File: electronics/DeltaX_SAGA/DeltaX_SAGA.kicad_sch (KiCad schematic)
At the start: 73 parts, among them J1 USB_B_Micro, J10 Motor3_Encoder, J11 M12, J12 M21, J13 M22, J14 M31, J15 M33, J16 Thrower+, J17 Thrower-, J2 Programmer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

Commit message: schematic updated
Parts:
- L1: value 7.6uH -> 6.8uH
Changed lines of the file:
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@@
       (effects (font (size 1.27 1.27)) (justify left))
     )
-    (property "Value" "7.6uH" (id 1) (at 232.6132 68.8594 90)
+    (property "Value" "6.8uH" (id 1) (at 232.6132 68.8594 90)
       (effects (font (size 1.27 1.27)) (justify left))
     )
@@
     )
     (path "/69cf5053-6b07-4bfe-8c3a-5438a0737fc8"
-      (reference "L1") (unit 1) (value "7.6uH") (footprint "SRP6060FA5R6M:SRP6060FA5R6M")
+      (reference "L1") (unit 1) (value "6.8uH") (footprint "SRP6060FA5R6M:SRP6060FA5R6M")
     )
     (path "/a41829a6-8151-41c8-b9a0-f89cf565cdea"

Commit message: Schematic updated
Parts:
- L1: value 6.8uH -> 5.6uH
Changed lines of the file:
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@@
       (effects (font (size 1.27 1.27)) (justify left))
     )
-    (property "Value" "6.8uH" (id 1) (at 232.6132 68.8594 90)
+    (property "Value" "5.6uH" (id 1) (at 232.6132 68.8594 90)
       (effects (font (size 1.27 1.27)) (justify left))
     )
@@
     )
     (path "/69cf5053-6b07-4bfe-8c3a-5438a0737fc8"
-      (reference "L1") (unit 1) (value "6.8uH") (footprint "SRP6060FA5R6M:SRP6060FA5R6M")
+      (reference "L1") (unit 1) (value "5.6uH") (footprint "SRP6060FA5R6M:SRP6060FA5R6M")
     )
     (path "/a41829a6-8151-41c8-b9a0-f89cf565cdea"

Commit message: Schematic updated
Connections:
- net +5VD: now also J3.2 (Pin_2); no longer J3.1 (Pin_1)
- net Servo_PWM_Isolated: now also J3.1 (Pin_1); no longer J3.2 (Pin_2)
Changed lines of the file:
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@@
     (stroke (width 0) (type default) (color 0 0 0 0))
   )
-  (wire (pts (xy 343.408 228.6) (xy 343.408 226.822))
+  (wire (pts (xy 338.836 228.6) (xy 338.836 225.2726))
     (stroke (width 0) (type default) (color 0 0 0 0))
   )
@@
     (stroke (width 0) (type default) (color 0 0 0 0))
   )
-  (wire (pts (xy 337.312 228.6) (xy 343.408 228.6))
+  (wire (pts (xy 337.312 231.14) (xy 343.408 231.14))
     (stroke (width 0) (type default) (color 0 0 0 0))
   )
@@
     (stroke (width 0) (type default) (color 0 0 0 0))
   )
+  (wire (pts (xy 338.836 225.2726) (xy 339.979 225.2726))
+    (stroke (width 0) (type default) (color 0 0 0 0))
+  )
   (wire (pts (xy 345.821 82.3976) (xy 345.821 84.963))
     (stroke (width 0) (type default) (color 0 0 0 0))
@@
   )
   (polyline (pts (xy 390.017 174.625) (xy 390.017 147.574))
+    (stroke (width 0) (type default) (color 0 0 0 0))
+  )
+  (wire (pts (xy 337.312 228.6) (xy 338.836 228.6))
     (stroke (width 0) (type default) (color 0 0 0 0))
   )
@@
     (effects (font (size 1.27 1.27)) (justify left bottom))
   )
-  (label "Servo_PWM_Isolated" (at 337.312 231.14 0)
-    (effects (font (size 1.27 1.27)) (justify left bottom))
+  (label "Servo_PWM_Isolated" (at 339.979 225.2726 0)
+    (effects (font (size 1 1)) (justify left bottom))
   )
   (label "Motor3_OUT1" (at 289.3568 41.7322 180)
@@
     (pin "2")
   )
-  (symbol (lib_id "power:+5VD") (at 343.408 226.822 0) (unit 1)
-    (in_bom yes) (on_board yes)
-    (property "Reference" "#PWR014" (id 0) (at 343.408 230.632 0)
-      (effects (font (size 1.27 1.27)) hide)
-    )
-    (property "Value" "+5VD" (id 1) (at 343.154 223.012 0))
-    (property "Footprint" "" (id 2) (at 343.408 226.822 0)
-      (effects (font (size 1.27 1.27)) hide)
-    )
-    (property "Datasheet" "" (id 3) (at 343.408 226.822 0)
-      (effects (font (size 1.27 1.27)) hide)
-    )
+  (symbol (lib_id "power:+5VD") (at 343.408 231.14 0) (unit 1)
+    (in_bom yes) (on_board yes)
+    (property "Reference" "#PWR014" (id 0) (at 343.408 234.95 0)
+      (effects (font (size 1.27 1.27)) hide)
+    )
+    (property "Value" "+5VD" (id 1) (at 343.154 227.33 0))
+    (property "Footprint" "" (id 2) (at 343.408 231.14 0)
+      (effects (font (size 1.27 1.27)) hide)
+    )
+    (property "Datasheet" "" (id 3) (at 343.408 231.14 0)
+      (effects (font (size 1.27 1.27)) hide)
+    )

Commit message: Labels and orientations of certain components updated in schematic
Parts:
- J10: value Motor3_Encoder -> M3_Encoder
- J16: value Thrower+ -> THRWR+
- J17: value Thrower- -> THRWR-
- J5: value Battery+ -> BAT+
- J6: value Thrower Signal -> Thrower
- J7: value Battery- -> BAT-
- J8: value Motor1_Encoder -> M1_Encoder
- J9: value Motor2_Encoder -> M2_Encoder
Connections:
- net Servo_PWM: now also U3.25 (PA15), U7.3 (INA1); no longer U3.7 (PA2), U8.2 (IN1)
- net Servo_PWM_Isolated: now also U7.14 (INB1); no longer U8.7 (OUT1)
- net Thrower_PWM: now also U3.7 (PA2), U8.2 (IN1); no longer U3.25 (PA15), U7.3 (INA1)
- net Thrower_PWM_Isolated: now also U8.7 (OUT1); no longer U7.14 (INB1)
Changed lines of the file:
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@@
     (effects (font (size 1.27 1.27)) (justify right bottom))
   )
-  (label "Thrower_PWM" (at 346.6846 42.3926 180)
+  (label "Thrower_PWM" (at 346.7354 126.746 180)
     (effects (font (size 1.27 1.27)) (justify right bottom))
   )
@@
     (effects (font (size 1.27 1.27)) (justify right bottom))
   )
-  (label "Thrower_PWM" (at 76.0984 219.6084 0)
-    (effects (font (size 1.27 1.27)) (justify left bottom))
+  (label "Thrower_PWM" (at 45.6184 214.5284 180)
+    (effects (font (size 1.27 1.27)) (justify right bottom))
   )
   (label "Motor3_DIR" (at 345.821 98.425 180)
@@
     (effects (font (size 1.27 1.27)) (justify left bottom))
   )
-  (label "Thrower_PWM_Isolated" (at 368.2746 42.3926 0)
+  (label "Thrower_PWM_Isolated" (at 367.0554 126.746 0)
     (effects (font (size 1.27 1.27)) (justify left bottom))
   )
@@
     (effects (font (size 1.27 1.27)) (justify right bottom))
   )
-  (label "Servo_PWM" (at 45.6184 214.5284 180)
-    (effects (font (size 1.27 1.27)) (justify right bottom))
+  (label "Servo_PWM" (at 76.0984 219.6084 0)
+    (effects (font (size 1.27 1.27)) (justify left bottom))
   )
   (label "Motor1_DIR" (at 76.0984 237.1344 0)
@@
     (effects (font (size 1.27 1.27)) (justify right bottom))
   )
-  (label "Servo_PWM_Isolated" (at 367.0554 126.746 0)
+  (label "Servo_PWM_Isolated" (at 368.2746 42.3926 0)
     (effects (font (size 1.27 1.27)) (justify left bottom))
   )
@@
     (effects (font (size 1.27 1.27)) (justify right bottom))
   )
-  (label "Servo_PWM" (at 346.7354 126.746 180)
+  (label "Servo_PWM" (at 346.6846 42.3926 180)
     (effects (font (size 1.27 1.27)) (justify right bottom))
   )
@@
       (effects (font (size 1.27 1.27)) (justify right))
     )
-    (property "Value" "Motor3_Encoder" (id 1) (at 369.062 150.876 0)
+    (property "Value" "M3_Encoder" (id 1) (at 369.062 150.876 0)
       (effects (font (size 1.27 1.27)) (justify right))
     )
@@
       (effects (font (size 0.8 0.8)) (justify left))
     )
-    (property "Value" "Thrower-" (id 1) (at 340.995 189.484 0)
+    (property "Value" "THRWR-" (id 1) (at 340.995 189.484 0)
       (effects (font (size 1.27 1.27)) (justify left))
     )
@@
       (effects (font (size 0.8 0.8)) (justify left))
     )
-    (property "Value" "Battery+" (id 1) (at 164.2618 41.529 0)
+    (property "Value" "BAT+" (id 1) (at 164.2618 41.529 0)
       (effects (font (size 1.27 1.27)) (justify left))
     )
@@
       (effects (font (size 1.27 1.27)) (justify right))
     )
-    (property "Value" "Motor2_Encoder" (id 1) (at 345.186 150.495 0)
+    (property "Value" "M2_Encoder" (id 1) (at 345.186 150.495 0)
       (effects (font (size 1.27 1.27)) (justify right))
     )
@@
       (effects (font (size 0.8 0.8)) (justify left))
     )
-    (property "Value" "Thrower+" (id 1) (at 340.9442 185.5978 0)
+    (property "Value" "THRWR+" (id 1) (at 340.9442 185.5978 0)
       (effects (font (size 1.27 1.27)) (justify left))
     )
@@
   (symbol (lib_id "Connector_Generic:Conn_02x02_Counter_Clockwise") (at 348.996 203.454 0) (unit 1)
     (in_bom yes) (on_board yes) (fields_autoplaced)
-    (property "Reference" "J6" (id 0) (at 350.266 196.342 0))
-    (property "Value" "Thrower Signal" (id 1) (at 350.266 198.882 0))
+    (property "Reference" "J6" (id 0) (at 350.266 196.85 0))
+    (property "Value" "Thrower" (id 1) (at 350.266 199.39 0))
     (property "Footprint" "Micro-MaTch215079-4:TE_7-215079-4" (id 2) (at 348.996 203.454 0)
       (effects (font (size 1.27 1.27)) hide)
@@
       (effects (font (size 1.27 1.27)) (justify right))
     )
-    (property "Value" "Motor1_Encoder" (id 1) (at 322.58 150.241 0)
+    (property "Value" "M1_Encoder" (id 1) (at 322.58 150.241 0)
       (effects (font (size 1.27 1.27)) (justify right))
     )
@@
       (effects (font (size 0.8 0.8)) (justify left))
     )
-    (property "Value" "Battery-" (id 1) (at 164.3126 45.4152 0)
+    (property "Value" "BAT-" (id 1) (at 164.3126 45.4152 0)
       (effects (font (size 1.27 1.27)) (justify left))
     )
@@
     )
     (path "/243d85bf-2c4c-45b0-9cab-ec50ea85f917"
-      (reference "J5") (unit 1) (value "Battery+") (footprint "1pinSMD:1PinSMD")
+      (reference "J5") (unit 1) (value "BAT+") (footprint "1pinSMD:1PinSMD")
     )
     (path "/be2cdfe9-b395-4bc1-b20e-5533fb8f2ec7"
-      (reference "J6") (unit 1) (value "Thrower Signal") (footprint "Micro-MaTch215079-4:TE_7-215079-4")
+      (reference "J6") (unit 1) (value "Thrower") (footprint "Micro-MaTch215079-4:TE_7-215079-4")
     )
     (path "/f0c56b83-4956-4f70-b2d3-f044d356fa34"
-      (reference "J7") (unit 1) (value "Battery-") (footprint "1pinSMD:1PinSMD")
+      (reference "J7") (unit 1) (value "BAT-") (footprint "1pinSMD:1PinSMD")
     )
     (path "/d5f450b4-5331-4602-9ead-55fd5f3dce29"
-      (reference "J8") (unit 1) (value "Motor1_Encoder") (footprint "Micro-MaTch215079-4:TE_7-215079-4")
+      (reference "J8") (unit 1) (value "M1_Encoder") (footprint "Micro-MaTch215079-4:TE_7-215079-4")
     )
     (path "/406cc448-cfa9-4f88-9d1b-651733518b56"
-      (reference "J9") (unit 1) (value "Motor2_Encoder") (footprint "Micro-MaTch215079-4:TE_7-215079-4")
+      (reference "J9") (unit 1) (value "M2_Encoder") (footprint "Micro-MaTch215079-4:TE_7-215079-4")
     )
     (path "/02c3a026-c130-412d-a72c-5fd2bdab5eb2"
-      (reference "J10") (unit 1) (value "Motor3_Encoder") (footprint "Micro-MaTch215079-4:TE_7-215079-4")
+      (reference "J10") (unit 1) (value "M3_Encoder") (footprint "Micro-MaTch215079-4:TE_7-215079-4")
     )
     (path "/e5ef77ee-abbd-4d5e-994a-dd6fe6346e26"
@@
     )
     (path "/b510d148-811f-4fa7-a0ac-0e64fe54363e"
-      (reference "J16") (unit 1) (value "Thrower+") (footprint "1pinSMD:1PinSMD")
+      (reference "J16") (unit 1) (value "THRWR+") (footprint "1pinSMD:1PinSMD")
     )
     (path "/21405553-e533-4dae-9b00-41345b6bfa18"
-      (reference "J17") (unit 1) (value "Thrower-") (footprint "1pinSMD:1PinSMD")
+      (reference "J17") (unit 1) (value "THRWR-") (footprint "1pinSMD:1PinSMD")
     )
     (path "/69cf5053-6b07-4bfe-8c3a-5438a0737fc8"

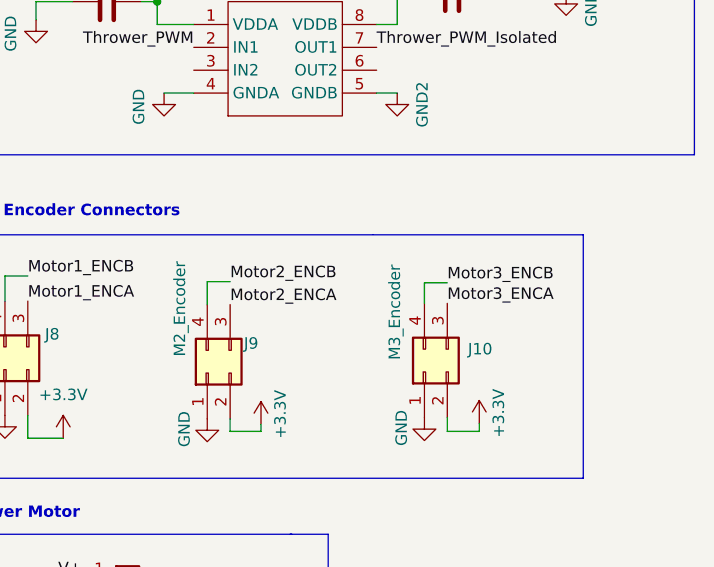
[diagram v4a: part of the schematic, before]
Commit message: PCB design updated with routing improvements
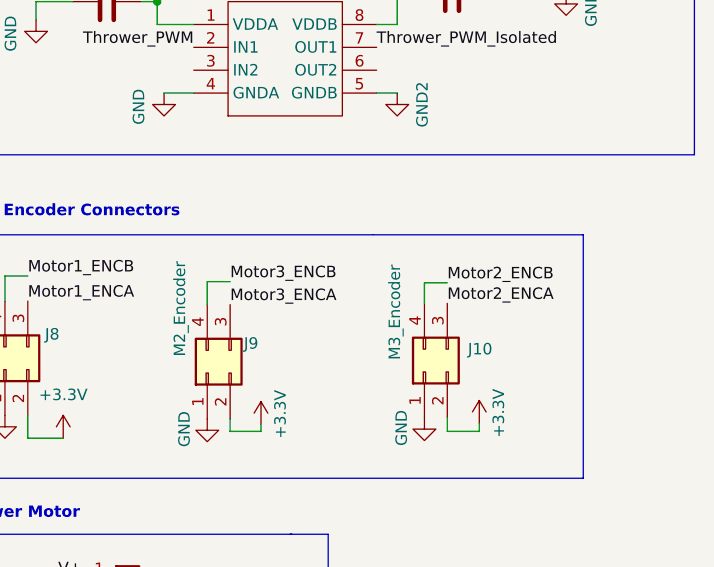
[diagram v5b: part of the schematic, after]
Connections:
- net Motor2_ENCA: now also J10.3 (Pin_3); no longer J9.3 (Pin_3)
- net Motor2_ENCB: now also J10.4 (Pin_4); no longer J9.4 (Pin_4)
- net Motor3_ENCA: now also J9.3 (Pin_3); no longer J10.3 (Pin_3)
- net Motor3_ENCB: now also J9.4 (Pin_4); no longer J10.4 (Pin_4)
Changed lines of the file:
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@@
     (effects (font (size 1.27 1.27)) (justify left bottom))
   )
-  (label "Motor3_ENCA" (at 374.904 155.194 0)
+  (label "Motor3_ENCA" (at 350.774 155.321 0)
     (effects (font (size 1.27 1.27)) (justify left bottom))
   )
@@
     (effects (font (size 1.27 1.27)) (justify left bottom))
   )
-  (label "Motor3_ENCB" (at 374.904 152.908 0)
+  (label "Motor3_ENCB" (at 350.774 152.781 0)
     (effects (font (size 1.27 1.27)) (justify left bottom))
   )
@@
     (effects (font (size 1.27 1.27)) (justify left bottom))
   )
-  (label "Motor2_ENCB" (at 350.774 152.781 0)
+  (label "Motor2_ENCB" (at 374.904 152.908 0)
     (effects (font (size 1.27 1.27)) (justify left bottom))
   )
@@
     (effects (font (size 1.27 1.27)) (justify right bottom))
   )
-  (label "Motor2_ENCA" (at 350.774 155.321 0)
-    (effects (font (size 1.27 1.27)) (justify left bottom))
-  )
+  (label "Motor2_ENCA" (at 374.904 155.194 0)
+    (effects (font (size 1.27 1.27)) (justify left bottom))
+  )
